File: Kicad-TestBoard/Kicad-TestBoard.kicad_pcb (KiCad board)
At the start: 2 copper layers, 50 x 100 mm, 35 parts, among them CON1 Power 6V-12V, J1 DB9 RS-232 Female, P1 Power 6V-12V, P2 Debug, P3 Debug, P4 Arduino, P5 AVR Programmer, P6 RS-232, Q1 Association, Q2 On_Sleep, Q3 Commissioning, SW1 Reset, SW2 Commissioning, U1 78L05, U2 MAX232

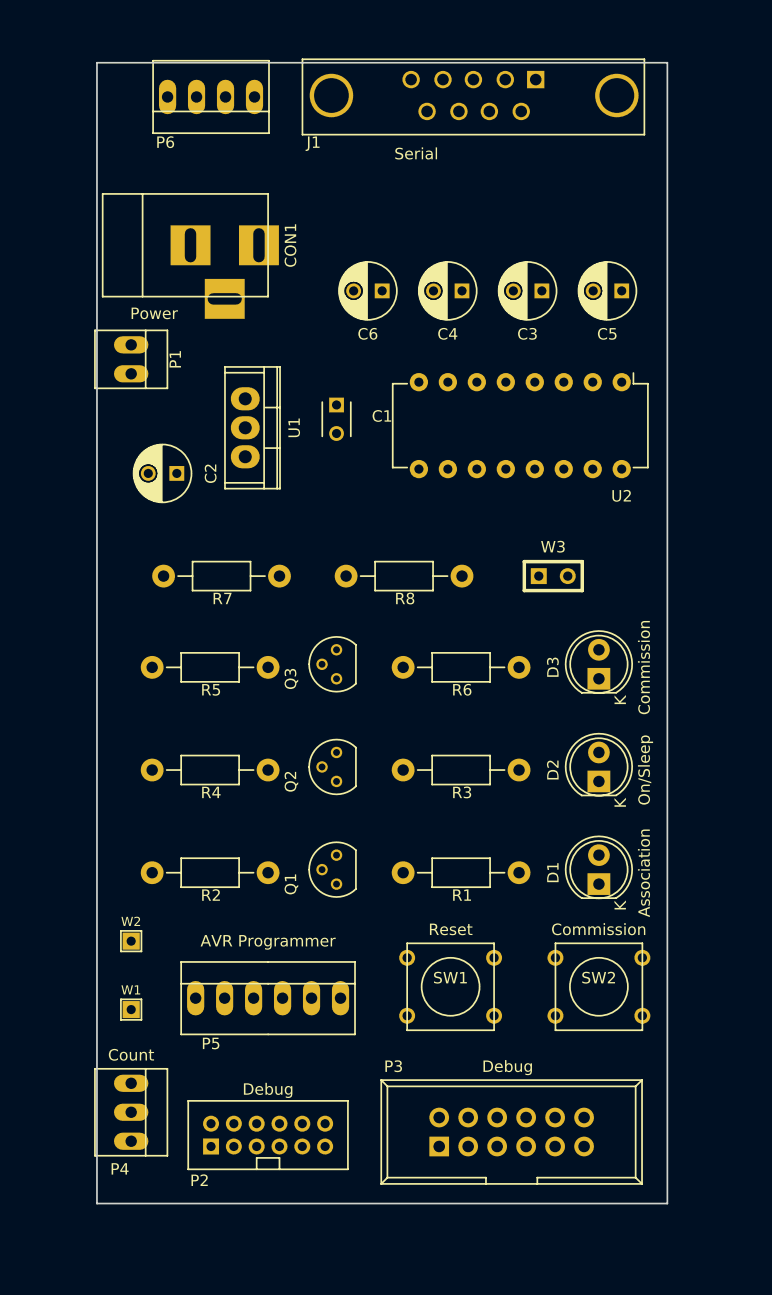
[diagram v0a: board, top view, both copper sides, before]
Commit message: Completion of test board. The 0.1" 12-pin debug connector removed as unnecessary and too complicating for the layout. PB switches adapted to smaller more common version available locally.
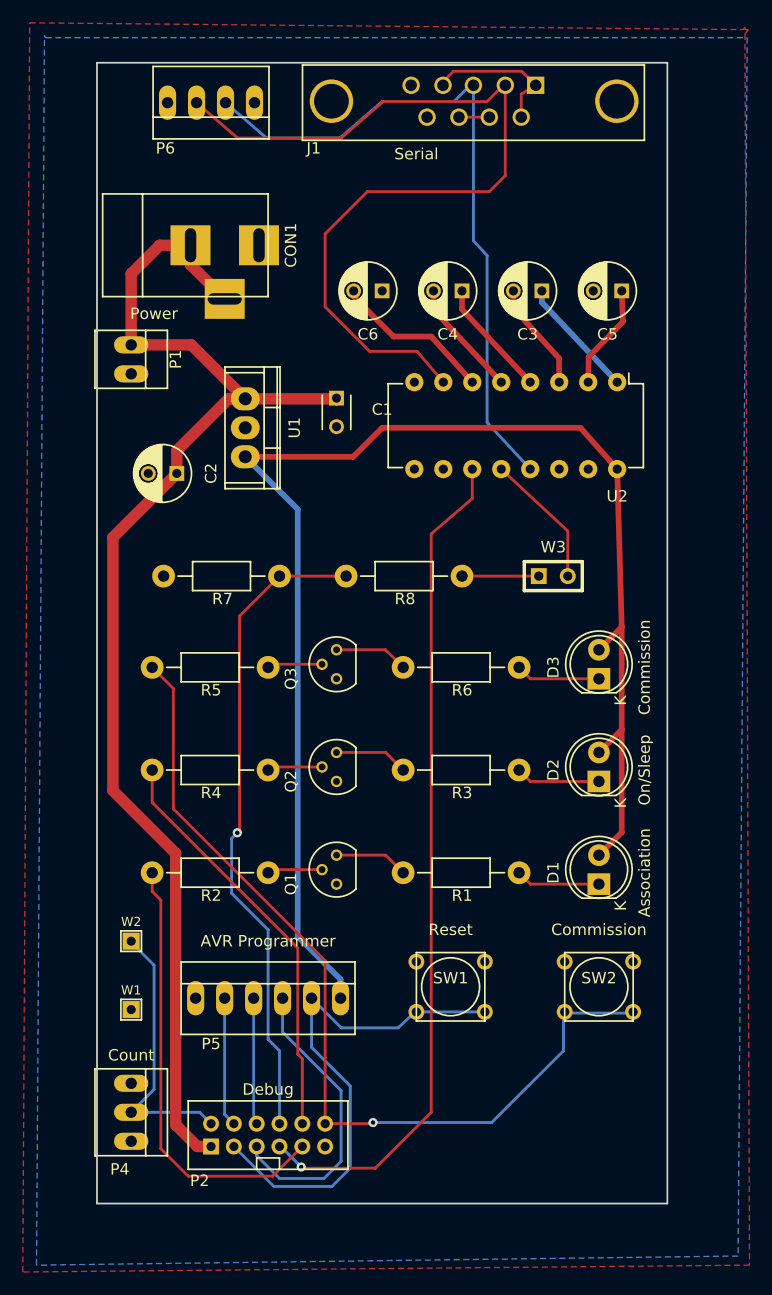
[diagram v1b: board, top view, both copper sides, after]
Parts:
- removed P3: Debug, Testboard:IDC_Header_Straight_12pins
- SW1, SW2: footprint Testboard:SW_PUSH_SMALL -> Testboard:SW_PUSH_TINY
- moved C1 0.60 mm to (171.0, 79.4)
- moved J1 0.50 mm to (183.0, 53.5)
- moved P6 0.50 mm to (160.0, 53.5)
- moved U2 0.40 mm to (195.6, 78.0)
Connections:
- net /Association renamed Net-(P2-Pad9)
- CON1 pad 3: Net-(CON1-Pad3) -> /Battery
- P2 pad 11: Net-(P2-Pad11) -> Earth
- P6 pad 1: VCC -> Net-(P6-Pad1)
- R7 pad 1: Net-(R7-Pad1) -> /Rx
- U2 pad 15: Net-(U2-Pad15) -> Earth
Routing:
- net VCC: track 0.00 -> 126.5 mm
- net /Battery: track 0.00 -> 114.1 mm
- net /Commissioning: track 0.00 -> 79.3 mm, vias 0 -> 1
- net Net-(J1-Pad2): track 0.00 -> 75.4 mm
- net /Tx: track 0.00 -> 74.1 mm, vias 0 -> 1
- net Net-(J1-Pad3): track 0.00 -> 60.3 mm
- net /Rx: track 0.00 -> 57.3 mm, vias 0 -> 1
- net /Reset: track 0.00 -> 45.3 mm
- net Net-(P2-Pad9): track 0.00 -> 39.0 mm
- net /On_Sleep: track 0.00 -> 36.5 mm
- net /SCK: track 0.00 -> 26.1 mm
- net /Count: track 0.00 -> 24.1 mm
- net Net-(C6-Pad2): track 0.00 -> 14.1 mm
- net Net-(J1-Pad1): track 0.00 -> 12.8 mm
- net Net-(U2-Pad12): track 0.00 -> 11.9 mm
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- added copper zone on B.Cu, net Earth
- added copper zone on F.Cu, net Earth
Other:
- board text removed: "Debug"

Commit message: Bedug interface board modify to add mounting holes.
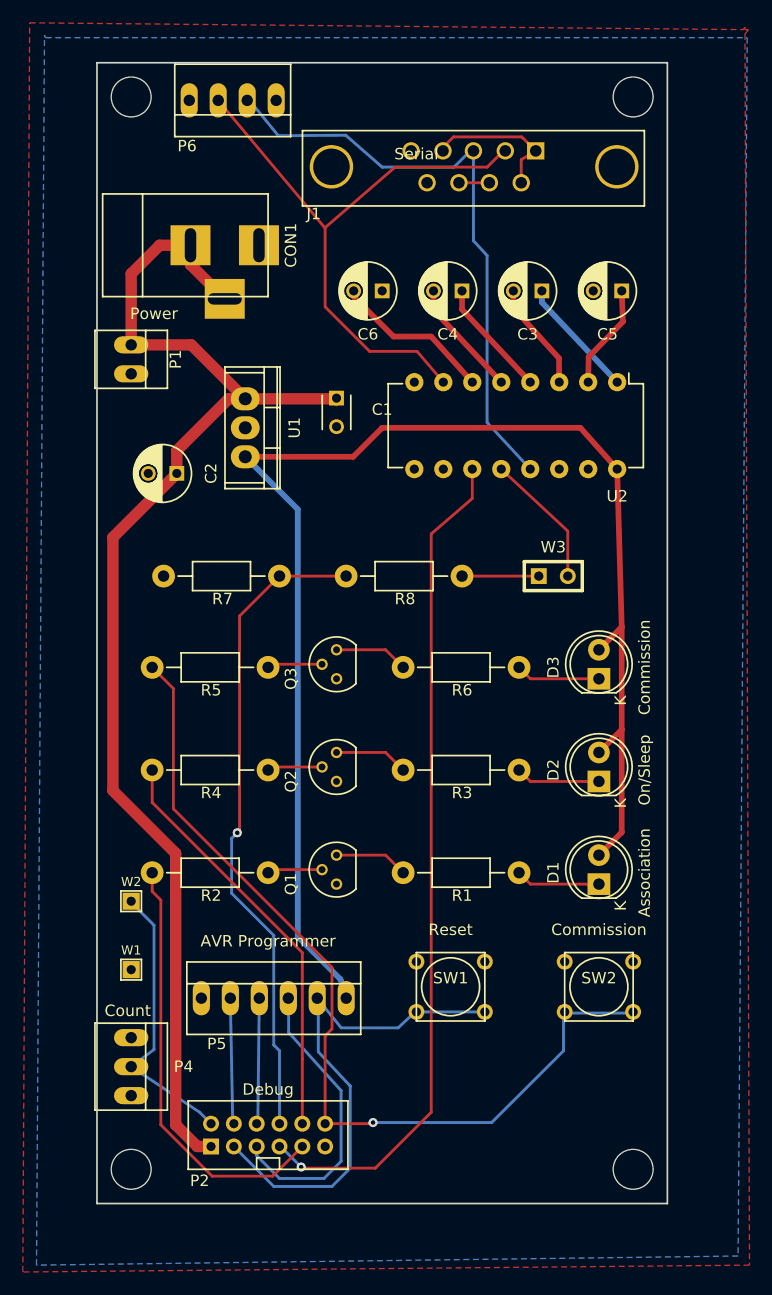
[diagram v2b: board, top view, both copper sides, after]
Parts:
- added ?: MountingHole_3-5mm, Testboard:MountingHole_3-5mm, F.Cu at (153.0, 53.0)
- added ?: MountingHole_3-5mm, Testboard:MountingHole_3-5mm, F.Cu at (153.0, 147.0)
- added ?: MountingHole_3-5mm, Testboard:MountingHole_3-5mm, F.Cu at (197.0, 147.0)
- added ?: MountingHole_3-5mm, Testboard:MountingHole_3-5mm, F.Cu at (197.0, 53.0)
- moved J1 5.75 mm to (183.0, 59.2)
- moved P4 4.00 mm to (153.0, 138.0)
- moved W1 3.50 mm to (153.0, 129.5)
- moved W2 3.50 mm to (153.0, 123.5)
- moved P6 1.91 mm to (161.9, 53.3)
- moved P5 0.50 mm to (165.5, 132.0)
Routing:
- net Net-(J1-Pad2): track 75.4 -> 53.1 mm
- net Net-(J1-Pad3): track 60.3 -> 52.9 mm
- net Net-(P2-Pad9): track 39.0 -> 37.8 mm
- net /Count: track 24.1 -> 25.0 mm
- net /Reset: track 45.3 -> 44.7 mm

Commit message: Testboard. Correct some footprint errors and change drill sizes to regular metric.
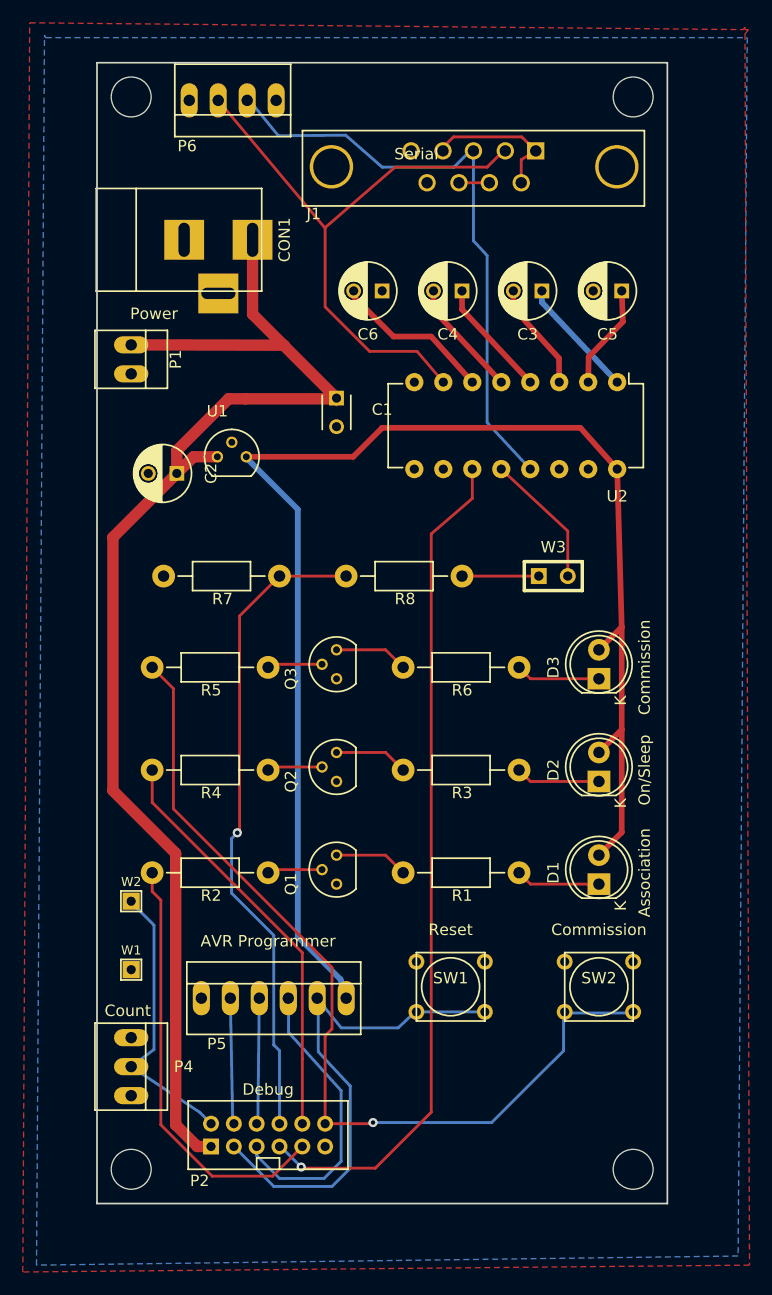
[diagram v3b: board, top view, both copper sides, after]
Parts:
- U1: footprint Testboard:TO-220 -> Testboard:TO-92_Molded_Narrow
- moved U1 3.53 mm to (160.6, 84.5), turned to 0 degrees
- moved CON1 0.74 mm to (157.4, 65.5)
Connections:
- CON1 pad 1: Earth -> /Battery
- CON1 pad 2: /Battery -> Earth
- CON1 pad 3: /Battery -> Earth
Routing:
- net /Battery: track 114.1 -> 118.2 mm

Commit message: Update of Testboard PCB and generation of gerbers.
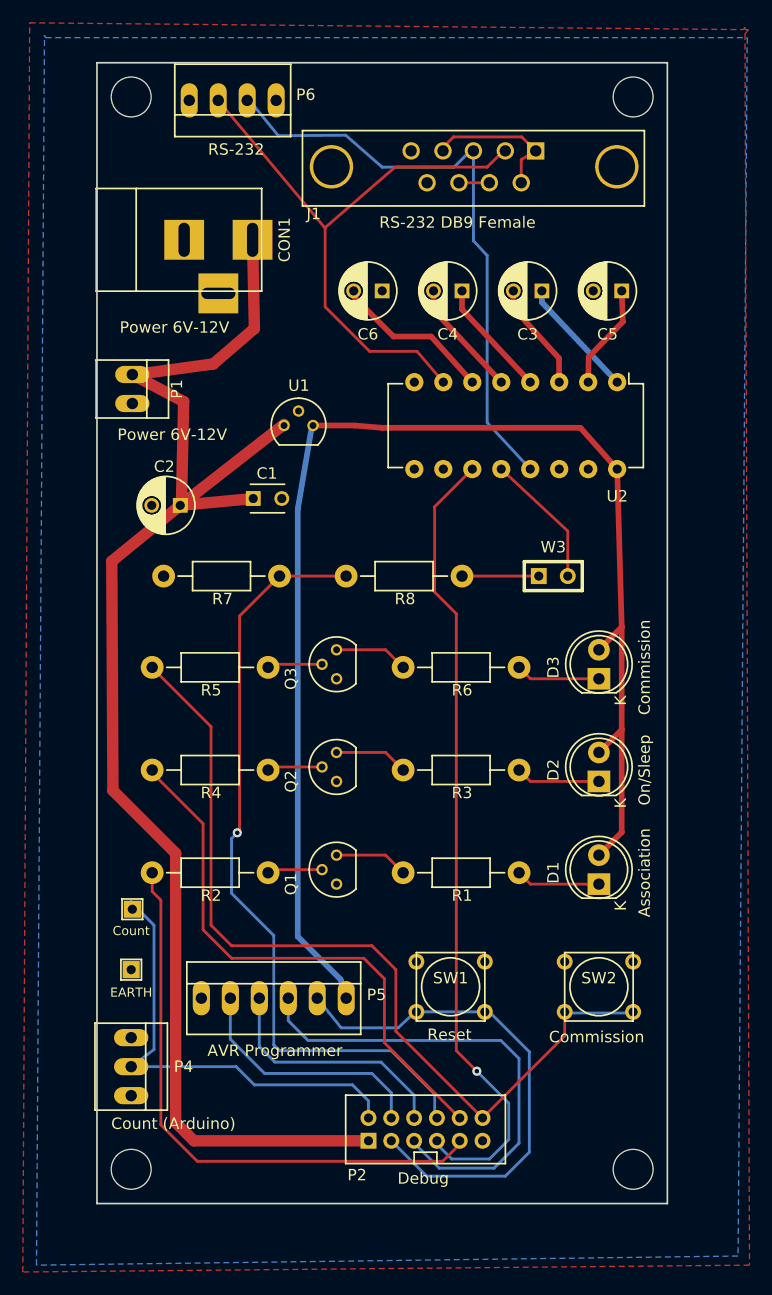
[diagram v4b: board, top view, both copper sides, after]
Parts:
- J1: value DB9 RS-232 Female -> RS-232 DB9 Female
- moved P2 13.8 mm to (178.8, 143.5)
- moved C1 11.4 mm to (163.7, 88.2), turned to 0 degrees
- moved U1 6.46 mm to (166.4, 81.8)
- moved C2 2.82 mm to (157.3, 88.8)
- moved P1 2.60 mm to (153.1, 78.6)
- moved Count 0.71 mm to (153.1, 124.2)
- renumbered W2 to Count, W1 to EARTH
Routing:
- net /SCK: track 25.7 -> 42.2 mm
- net /Count: track 25.0 -> 39.9 mm
- net Net-(P2-Pad9): track 37.8 -> 50.3 mm
- net /On_Sleep: track 36.5 -> 48.5 mm
- net /MOSI: track 10.9 -> 21.9 mm
- net /Battery: track 118.2 -> 129.1 mm
- net /Rx: track 57.3 -> 68.0 mm
- net /MISO: track 10.9 -> 21.6 mm
- net VCC: track 126.6 -> 120.6 mm
- net /Tx: track 74.1 -> 70.7 mm
- net /Commissioning: track 79.8 -> 77.2 mm, vias 1 -> 0
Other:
- board text added: "Count (Arduino)"
- board text added: "Power 6V-12V"
- board text added: "RS-232"
- board text added: "RS-232 DB9 Female"
- board text removed: "Count"
- board text removed: "Power"
- board text removed: "Serial"

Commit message: Corrections to Testboard PCB. - Incorrect Tx wiring to MAX232 - Make correct allocations of footprints in schematic - Add some extra text including title, version, author, date.
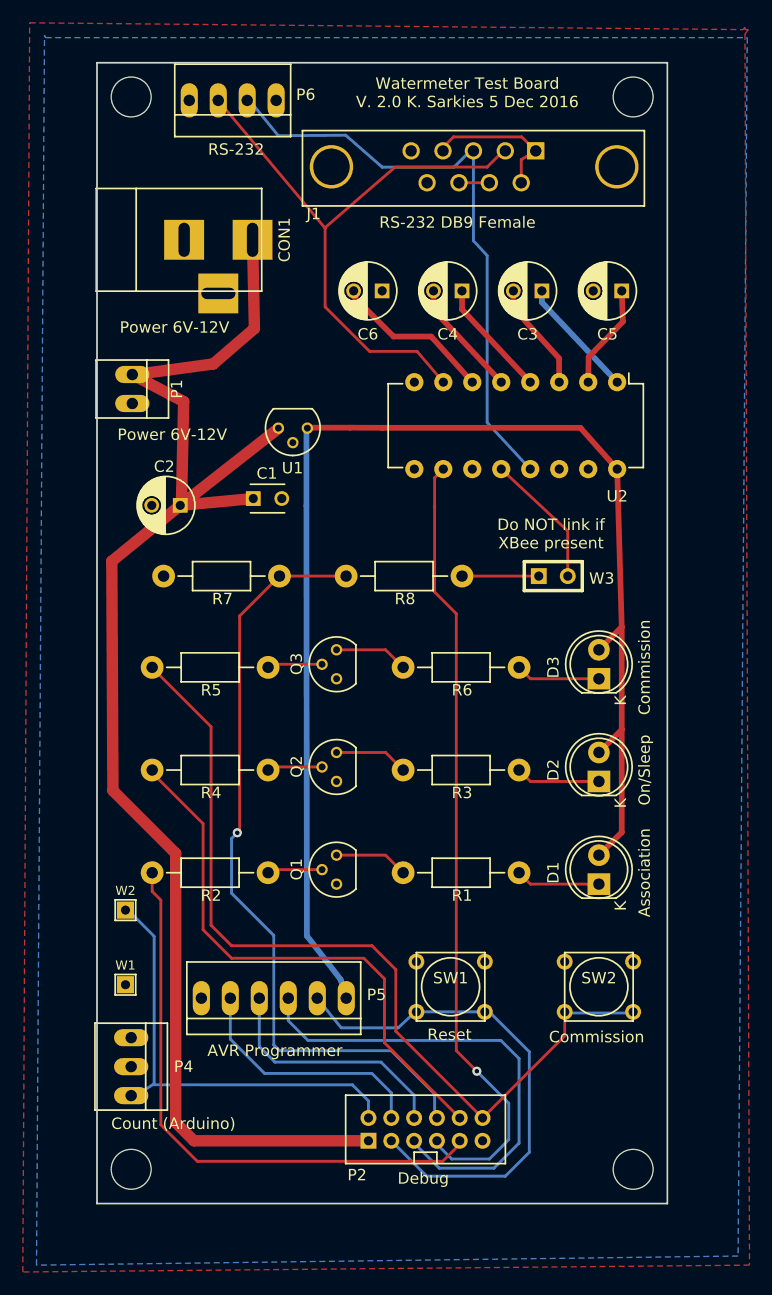
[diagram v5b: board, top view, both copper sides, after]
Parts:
- removed Count, EARTH: TEST_1P, Testboard:SIL-1
- added W1: TEST_1P, Testboard:SIL-1, F.Cu at (152.5, 130.8)
- added W2: TEST_1P, Testboard:SIL-1, F.Cu at (152.5, 124.3)
- J1: value RS-232 DB9 Female -> DB9 RS-232 Female
- U1: footprint Testboard:TO-92_Molded_Narrow -> Testboard:TO-92_78L05
- moved U1 2.05 mm to (168.4, 82.0), turned to 180 degrees
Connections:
- P4 pad 1: Net-(P4-Pad1) -> Earth
- P4 pad 2: /Count -> Net-(P4-Pad2)
- P4 pad 3: Earth -> /Count
- U2 pad 10: Net-(U2-Pad10) -> /Tx
- U2 pad 11: /Tx -> Net-(U2-Pad11)
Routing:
- net /Tx: track 70.7 -> 69.6 mm
- net /Count: track 39.9 -> 39.1 mm
- net /Battery: track 129.1 -> 128.5 mm
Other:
- board text added: "Do NOT link if XBee present"
- board text added: "Watermeter Test Board V. 2.0 K. Sarkies 5 Dec 2016"
